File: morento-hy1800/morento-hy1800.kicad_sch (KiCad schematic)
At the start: 34 parts, among them J1 DC, J2 Motor, J3 FLZ, Q2 S8050, SW1 Power/Mode Button, U1 HT7550-1, U3 ATHYC942 24C02N

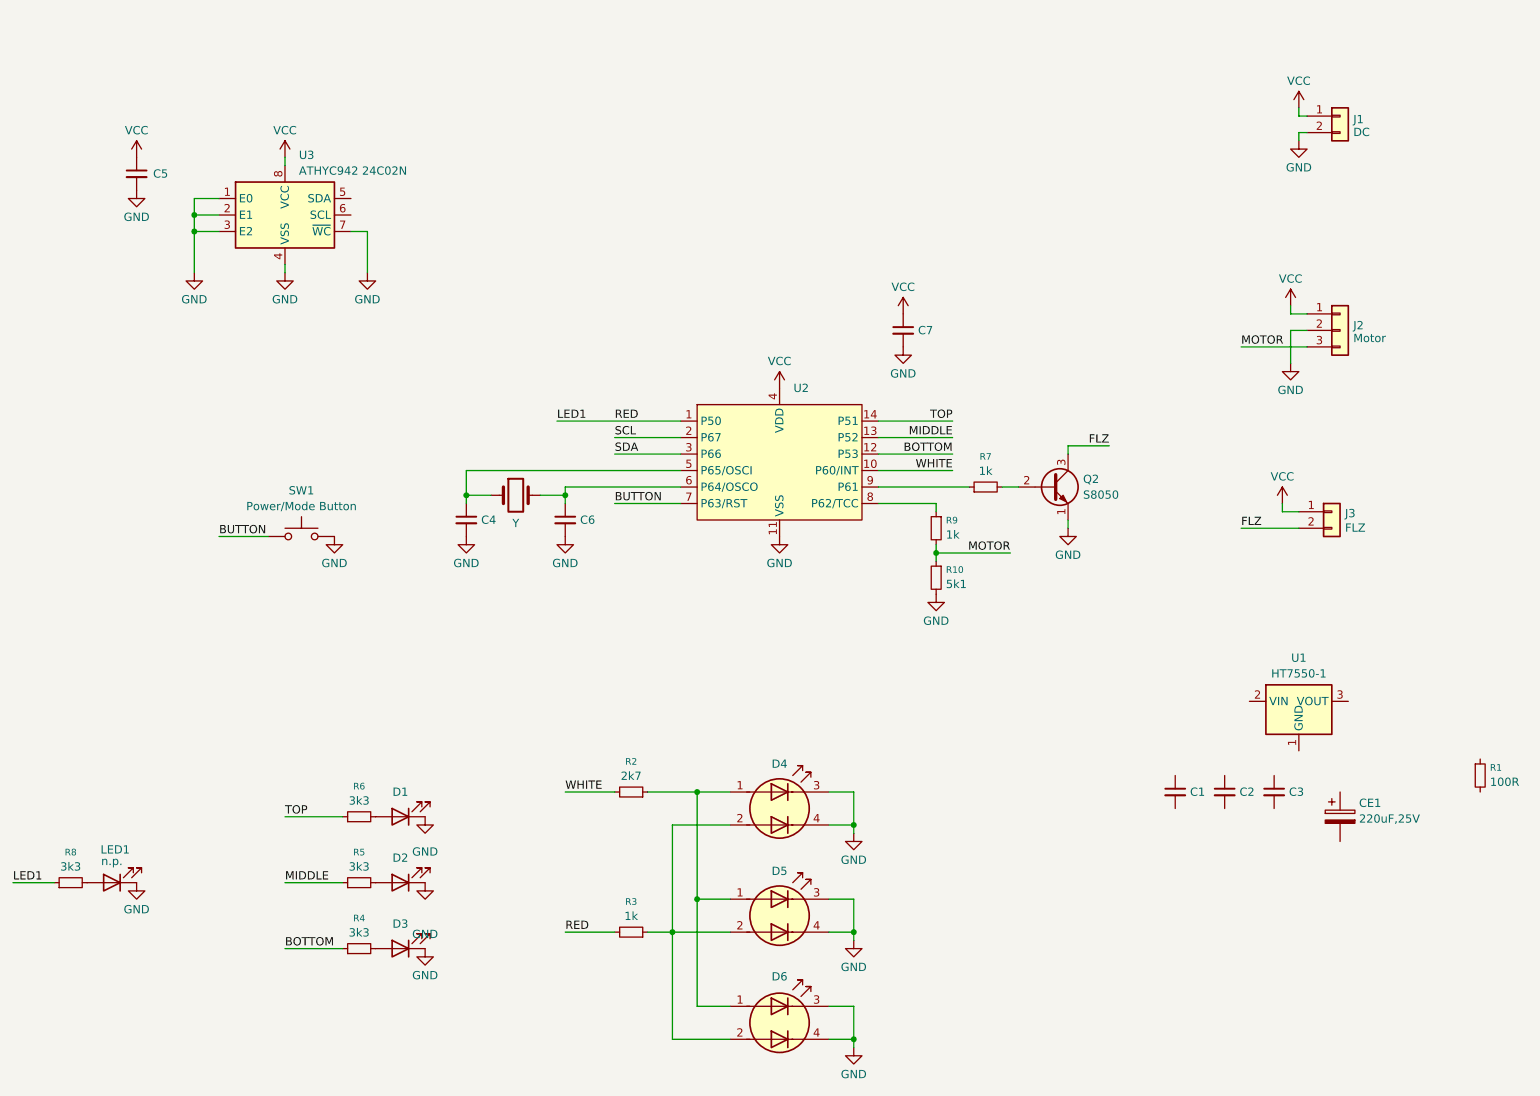
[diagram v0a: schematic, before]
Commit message: Drafting ESP32-C3 SuperMini replacement
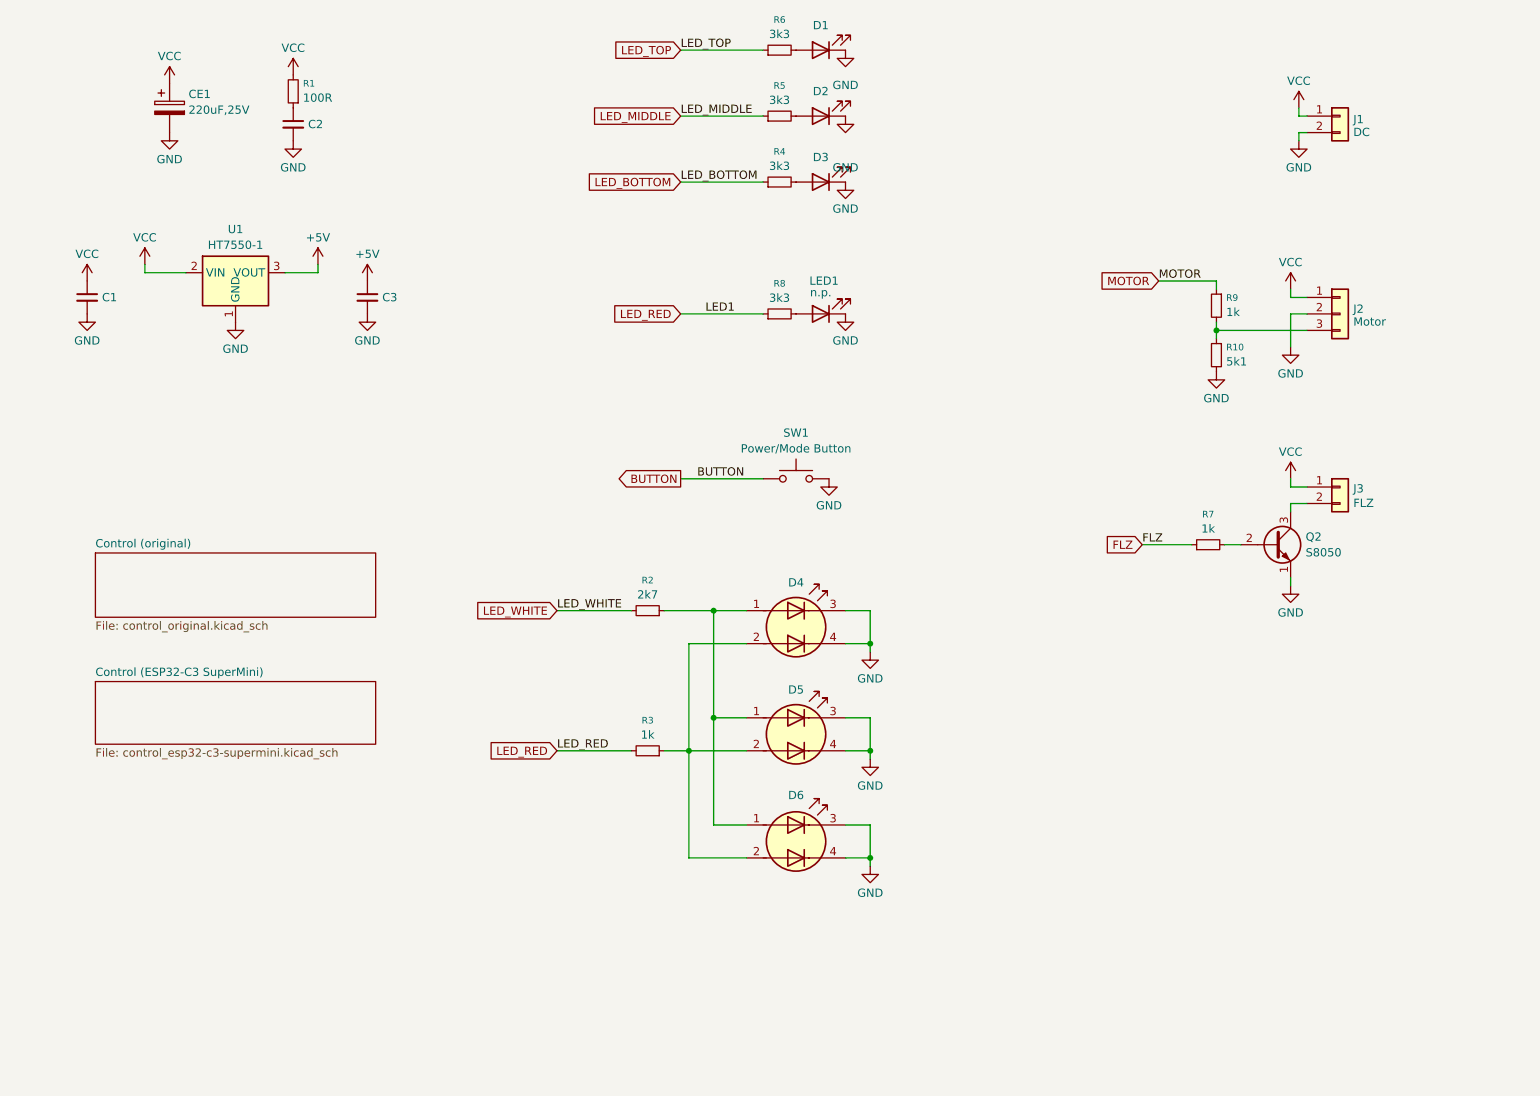
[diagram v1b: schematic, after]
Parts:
- removed C4, C5, C6, C7: C_Small, symbol Device:C_Small
- removed U2: ~, symbol morento:EM78P153E
- removed U3: ATHYC942 24C02N, Package_SO:SOIC-8_3.9x4.9mm_P1.27mm, symbol Memory_EEPROM:M24C02-FMN
- removed Y: Crystal, symbol Device:Crystal
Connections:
- net FLZ: now also R7.1; no longer J3.2 (Pin_2), Q2.3 (C)
- net GND: now also C1.2, C2.2, C3.2, CE1.2, U1.1 (GND)
- net MOTOR: now also R9.1; no longer J2.3 (Pin_3), R10.1, R9.2
- net VCC: now also C1.1, CE1.1, R1.2, U1.2 (VIN)
- net +5V: now reaches U1.3 (VOUT)
- net +5V: now also C3.1
- net at R1.1: now also C2.1
- net BOTTOM renamed LED_BOTTOM
- net LED1 renamed LED_RED
- net MIDDLE renamed LED_MIDDLE
- net TOP renamed LED_TOP
- net WHITE renamed LED_WHITE
- new net: J2.3 (Pin_3), R10.1, R9.2
- new net: J3.2 (Pin_2), Q2.3 (C)
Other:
- added sheet Control (ESP32-C3 SuperMini) (control_esp32-c3-supermini.kicad_sch)
- added sheet Control (original) (control_original.kicad_sch)
- moved on the sheet: C1, C2, C3, CE1, D1, D2, D3, D4, D5, D6, J2, J3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
